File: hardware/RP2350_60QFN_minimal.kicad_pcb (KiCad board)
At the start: 2 copper layers, 52 x 51 mm, 43 parts, among them J1 USB_B_Micro, J2 Conn_02x18_Odd_Even, J3 Conn_02x18_Odd_Even, J4 SM03B-SRSS-TB, SW1 SW_Push, SW2 SW_Push, U1 RP2350_60QFN, U2 NCP1117-3.3_SOT223, U3 W25Q128JVS, Y1 ABM8-272-T3

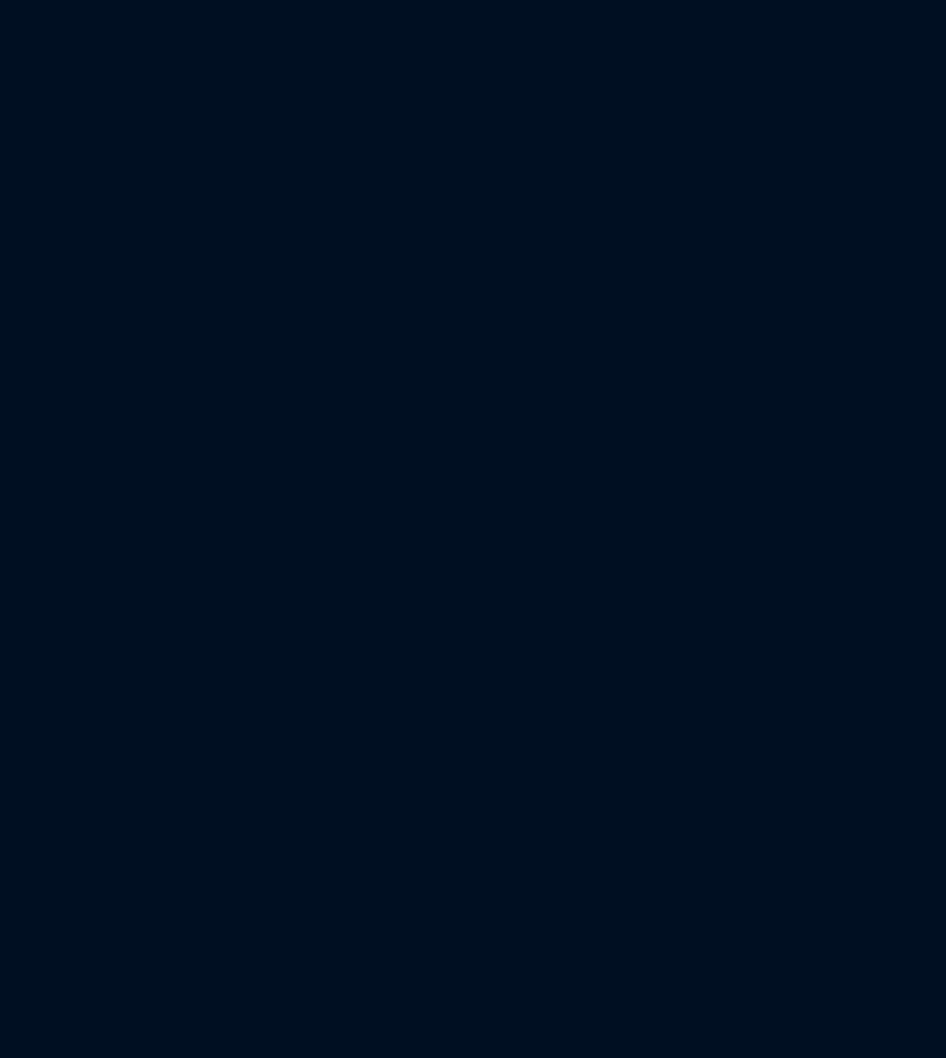
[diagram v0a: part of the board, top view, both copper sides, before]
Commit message: added footprints
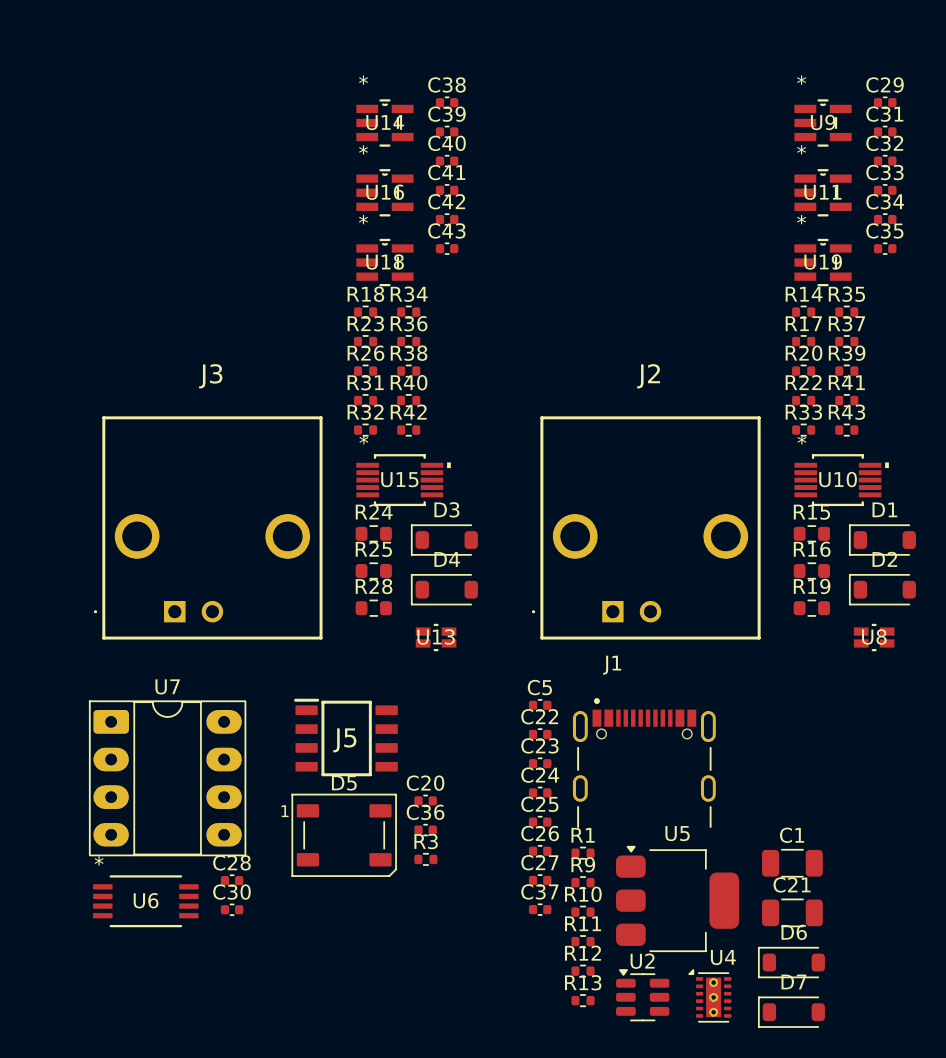
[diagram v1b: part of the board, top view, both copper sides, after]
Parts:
- added C1: 10u, Capacitor_SMD:C_1206_3216Metric, F.Cu at (262.3, 126.0)
- added C20: 100n, Capacitor_SMD:C_0402_1005Metric, F.Cu at (237.5, 121.7)
- added C21: 10u, Capacitor_SMD:C_1206_3216Metric, F.Cu at (262.3, 129.3)
- added C22: 1u, Capacitor_SMD:C_0402_1005Metric, F.Cu at (245.2, 117.3)
- added C23: 2.2u, Capacitor_SMD:C_0402_1005Metric, F.Cu at (245.2, 119.2)
- added C24: 2.2u, Capacitor_SMD:C_0402_1005Metric, F.Cu at (245.2, 121.2)
- added C25: 2.2u, Capacitor_SMD:C_0402_1005Metric, F.Cu at (245.2, 123.2)
- added C26: 100n, Capacitor_SMD:C_0402_1005Metric, F.Cu at (245.2, 125.1)
- added C27: 1u, Capacitor_SMD:C_0402_1005Metric, F.Cu at (245.2, 127.1)
- added C28: 100n, Capacitor_SMD:C_0402_1005Metric, F.Cu at (224.4, 127.1)
- added C29: 10n, Capacitor_SMD:C_0402_1005Metric, F.Cu at (268.5, 74.6)
- added C30: 100n, Capacitor_SMD:C_0402_1005Metric, F.Cu at (224.4, 129.1)
- added C31: 100n, Capacitor_SMD:C_0402_1005Metric, F.Cu at (268.5, 76.6)
- added C32: 100n, Capacitor_SMD:C_0402_1005Metric, F.Cu at (268.5, 78.6)
- added C33: 100n, Capacitor_SMD:C_0402_1005Metric, F.Cu at (268.5, 80.5)
- added C34: 100n, Capacitor_SMD:C_0402_1005Metric, F.Cu at (268.5, 82.5)
- added C35: 30p, Capacitor_SMD:C_0402_1005Metric, F.Cu at (268.5, 84.5)
- added C36: 100n, Capacitor_SMD:C_0402_1005Metric, F.Cu at (237.5, 123.7)
- added C37: 1u, Capacitor_SMD:C_0402_1005Metric, F.Cu at (245.2, 129.1)
- added C38: 10n, Capacitor_SMD:C_0402_1005Metric, F.Cu at (239.0, 74.6)
- added C39: 100n, Capacitor_SMD:C_0402_1005Metric, F.Cu at (239.0, 76.6)
- added C40: 100n, Capacitor_SMD:C_0402_1005Metric, F.Cu at (239.0, 78.6)
- added C41: 100n, Capacitor_SMD:C_0402_1005Metric, F.Cu at (239.0, 80.5)
- added C42: 100n, Capacitor_SMD:C_0402_1005Metric, F.Cu at (239.0, 82.5)
- added C43: 30p, Capacitor_SMD:C_0402_1005Metric, F.Cu at (239.0, 84.5)
- added C5: 4.7u, Capacitor_SMD:C_0402_1005Metric, F.Cu at (245.2, 115.3)
- added D1: D, Diode_SMD:D_SOD-123, F.Cu at (268.5, 104.1)
- added D2: D, Diode_SMD:D_SOD-123, F.Cu at (268.5, 107.5)
- added D3: D, Diode_SMD:D_SOD-123, F.Cu at (238.9, 104.1)
- added D4: D, Diode_SMD:D_SOD-123, F.Cu at (238.9, 107.5)
- added D5: WS2812B, LED_SMD:LED_WS2812B_PLCC4_5.0x5.0mm_P3.2mm, F.Cu at (232.0, 124.1)
- added D6: 2.4V, Diode_SMD:D_SOD-123, F.Cu at (262.4, 132.7)
- added D7: 2.4V, Diode_SMD:D_SOD-123, F.Cu at (262.4, 136.0)
- added J1: UJ20-C-H-G-SMT-2A-P16-TR, USBC_UJ20-C-H-G-SMT-1-P16-TR:SAMESKY_UJ20-C-H-G-SMT-1-P16-TR, F.Cu at (252.3, 123.5)
- added J2: 73101-0570, BNC:731010570, F.Cu at (250.1, 109.0)
- added J3: 73101-0570, BNC:731010570, F.Cu at (220.6, 109.0)
- added J5: 4677, PSRAM_Adafruit_4677:SOIC127P600X175-8N, F.Cu at (232.2, 117.5)
- added R1: 5.1k, Resistor_SMD:R_0402_1005Metric, F.Cu at (248.1, 125.3)
- added R10: 18.7k, Resistor_SMD:R_0402_1005Metric, F.Cu at (248.1, 129.2)
- added R11: 50k, Resistor_SMD:R_0402_1005Metric, F.Cu at (248.1, 131.2)
- added R12: 17.8k, Resistor_SMD:R_0402_1005Metric, F.Cu at (248.1, 133.2)
- added R13: 50k, Resistor_SMD:R_0402_1005Metric, F.Cu at (248.1, 135.2)
- added R14: 200, Resistor_SMD:R_0402_1005Metric, F.Cu at (263.0, 88.8)
- added R15: 1M, Resistor_SMD:R_0603_1608Metric, F.Cu at (263.6, 103.7)
- added R16: 320, Resistor_SMD:R_0603_1608Metric, F.Cu at (263.6, 106.2)
- added R17: 1k, Resistor_SMD:R_0402_1005Metric, F.Cu at (263.0, 90.8)
- added R18: 0, Resistor_SMD:R_0402_1005Metric, F.Cu at (233.5, 88.8)
- added R19: 51, Resistor_SMD:R_0603_1608Metric, F.Cu at (263.6, 108.7)
- added R20: 0, Resistor_SMD:R_0402_1005Metric, F.Cu at (263.0, 92.7)
- added R22: 1k, Resistor_SMD:R_0402_1005Metric, F.Cu at (263.0, 94.7)
- added R23: 200, Resistor_SMD:R_0402_1005Metric, F.Cu at (233.5, 90.8)
- added R24: 1M, Resistor_SMD:R_0603_1608Metric, F.Cu at (234.0, 103.7)
- added R25: 320, Resistor_SMD:R_0603_1608Metric, F.Cu at (234.0, 106.2)
- added R26: 1k, Resistor_SMD:R_0402_1005Metric, F.Cu at (233.5, 92.7)
- added R28: 51, Resistor_SMD:R_0603_1608Metric, F.Cu at (234.0, 108.7)
- added R3: 100k, Resistor_SMD:R_0402_1005Metric, F.Cu at (237.5, 125.7)
- added R31: 1k, Resistor_SMD:R_0402_1005Metric, F.Cu at (233.5, 94.7)
- added R32: 470, Resistor_SMD:R_0402_1005Metric, F.Cu at (233.5, 96.7)
- added R33: 470, Resistor_SMD:R_0402_1005Metric, F.Cu at (263.0, 96.7)
- added R34: 100k, Resistor_SMD:R_0402_1005Metric, F.Cu at (236.4, 88.8)
- added R35: 100k, Resistor_SMD:R_0402_1005Metric, F.Cu at (265.9, 88.8)
- added R36: 200k, Resistor_SMD:R_0402_1005Metric, F.Cu at (236.4, 90.8)
- added R37: 200k, Resistor_SMD:R_0402_1005Metric, F.Cu at (265.9, 90.8)
- added R38: 200k, Resistor_SMD:R_0402_1005Metric, F.Cu at (236.4, 92.7)
- added R39: 200k, Resistor_SMD:R_0402_1005Metric, F.Cu at (265.9, 92.7)
- added R40: 100k, Resistor_SMD:R_0402_1005Metric, F.Cu at (236.4, 94.7)
- added R41: 100k, Resistor_SMD:R_0402_1005Metric, F.Cu at (265.9, 94.7)
- added R42: 100k, Resistor_SMD:R_0402_1005Metric, F.Cu at (236.4, 96.7)
- added R43: 100k, Resistor_SMD:R_0402_1005Metric, F.Cu at (265.9, 96.7)
- added R9: 5.1k, Resistor_SMD:R_0402_1005Metric, F.Cu at (248.1, 127.3)
- added U10: ADG621BRMZ, ADG621BRMZ:RM_10_ADI, F.Cu at (265.3, 100.1)
- added U11: ~, OPA320:DBV5, F.Cu at (264.3, 80.7)
- added U13: TLP3441TP_F, TLP3441:VSON4_TOS, F.Cu at (238.2, 110.7)
- added U14: ~, OPA320:DBV5, F.Cu at (234.8, 76.0)
- added U15: ADG621BRMZ, ADG621BRMZ:RM_10_ADI, F.Cu at (235.8, 100.1)
- added U16: ~, OPA320:DBV5, F.Cu at (234.8, 80.7)
- added U18: ~, OPA320:DBV5, F.Cu at (234.8, 85.4)
- added U19: ~, OPA320:DBV5, F.Cu at (264.3, 85.4)
- added U2: REF35330QDBVR, Package_TO_SOT_SMD:SOT-23-6, F.Cu at (252.2, 135.0)
- added U4: LM27762, Package_SON:WSON-12-1EP_3x2mm_P0.5mm_EP1x2.65_ThermalVias, F.Cu at (256.9, 135.0)
- added U5: NCP1117-3.3_SOT223, Package_TO_SOT_SMD:SOT-223-3_TabPin2, F.Cu at (254.5, 128.5)
- added U6: MCP47FEB02A0T-E/ST, MCP47FE:TSSOP8_ST_MCH, F.Cu at (218.6, 128.5)
- added U7: Opamp_Dual, Package_DIP:DIP-8_W7.62mm_Socket_LongPads, F.Cu at (216.3, 116.4)
- added U8: TLP3441TP_F, TLP3441:VSON4_TOS, F.Cu at (267.8, 110.7)
- added U9: ~, OPA320:DBV5, F.Cu at (264.3, 76.0)
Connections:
- R6 pad 1: /QSPI_SS -> /~{FLASH_CS}
- U1 pad 10: /GPIO7 -> /TRIG_SCL
- U1 pad 12: /GPIO8 -> /~{PSRAM_CS}
- U1 pad 13: /GPIO9 -> /LED_DATA
- U1 pad 14: /GPIO10 -> /CHA_SELC
- U1 pad 15: /GPIO11 -> /CHA_SELR1
- U1 pad 16: /GPIO12 -> /CHA_SELR2
- U1 pad 17: /GPIO13 -> /CHB_SELC
- U1 pad 18: /GPIO14 -> /CHB_SELR1
- U1 pad 19: /GPIO15 -> /CHB_SELR2
- U1 pad 2: /GPIO0 -> unconnected-(U1-GPIO0-Pad2)
- U1 pad 27: /GPIO16 -> unconnected-(U1-GPIO16-Pad27)
- U1 pad 28: /GPIO17 -> unconnected-(U1-GPIO17-Pad28)
- U1 pad 29: /GPIO18 -> unconnected-(U1-GPIO18-Pad29)
- U1 pad 3: /GPIO1 -> unconnected-(U1-GPIO1-Pad3)
- U1 pad 31: /GPIO19 -> unconnected-(U1-GPIO19-Pad31)
- U1 pad 32: /GPIO20 -> /CHA_TRIG
- U1 pad 33: /GPIO21 -> /CHB_TRIG
- U1 pad 34: /GPIO22 -> unconnected-(U1-GPIO22-Pad34)
- U1 pad 35: /GPIO23 -> unconnected-(U1-GPIO23-Pad35)
- U1 pad 36: /GPIO24 -> unconnected-(U1-GPIO24-Pad36)
- U1 pad 37: /GPIO25 -> unconnected-(U1-GPIO25-Pad37)
- U1 pad 4: /GPIO2 -> unconnected-(U1-GPIO2-Pad4)
- U1 pad 40: /GPIO26_ADC0 -> /CHA_ADC
- U1 pad 41: /GPIO27_ADC1 -> /CHB_ADC
- U1 pad 42: /GPIO28_ADC2 -> unconnected-(U1-GPIO28_ADC2-Pad42)
- U1 pad 43: /GPIO29_ADC3 -> unconnected-(U1-GPIO29_ADC3-Pad43)
- U1 pad 44: +3V3 -> /VREF
- U1 pad 5: /GPIO3 -> unconnected-(U1-GPIO3-Pad5)
- U1 pad 60: /QSPI_SS -> /~{FLASH_CS}
- U1 pad 7: /GPIO4 -> unconnected-(U1-GPIO4-Pad7)
- U1 pad 8: /GPIO5 -> unconnected-(U1-GPIO5-Pad8)
- U1 pad 9: /GPIO6 -> /TRIG_SDA
- U3 pad 1: /FLASH_SS -> /~{FLASH_CS}
